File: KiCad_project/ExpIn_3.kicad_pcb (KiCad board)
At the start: 2 copper layers, 41 x 27 mm, 30 parts, among them J1 NMJ6HCD2, J2 Conn_01x08_MountingPin, J3 Conn_01x02_MountingPin, SW1 SW_Push, U1 74HC4066, U2 MCP6001-OT, U3 MCP4018T-103E/LT, U5 USBLC6-2SC6

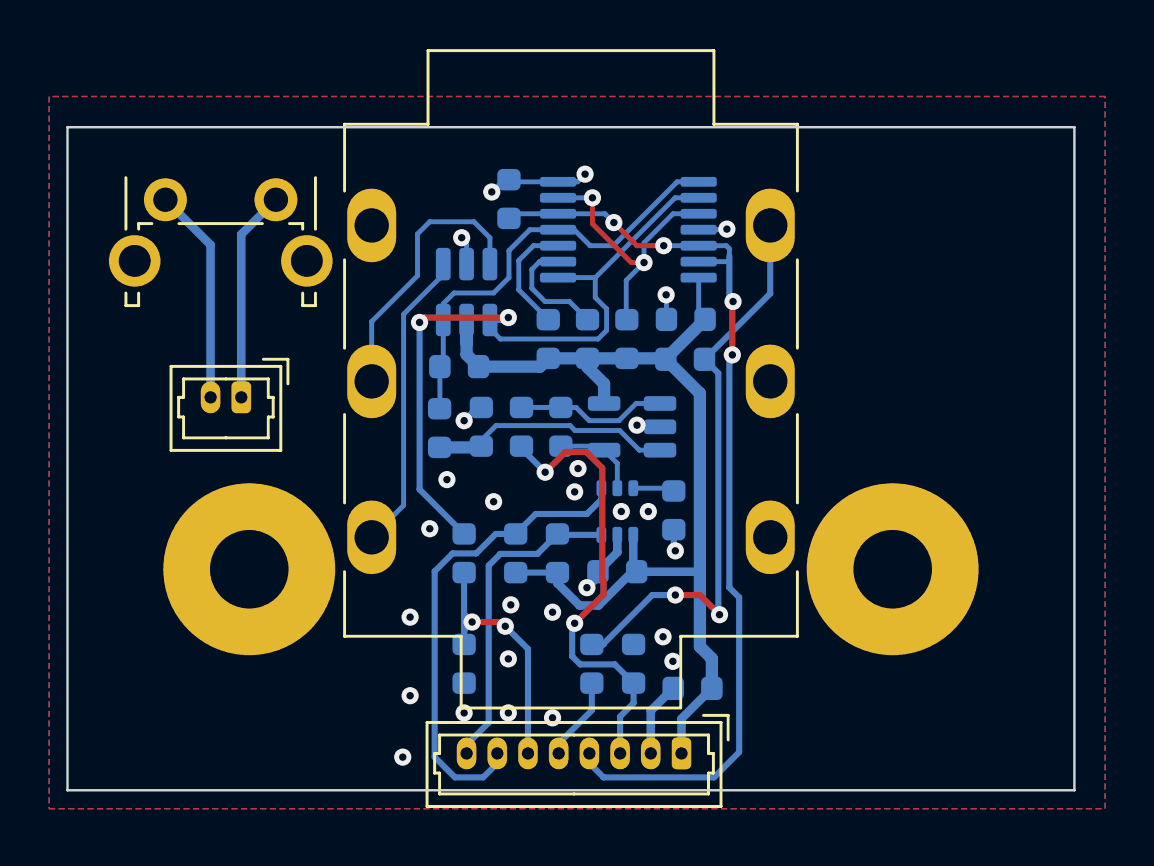
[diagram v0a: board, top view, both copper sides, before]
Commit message: SMT connectors, gain control
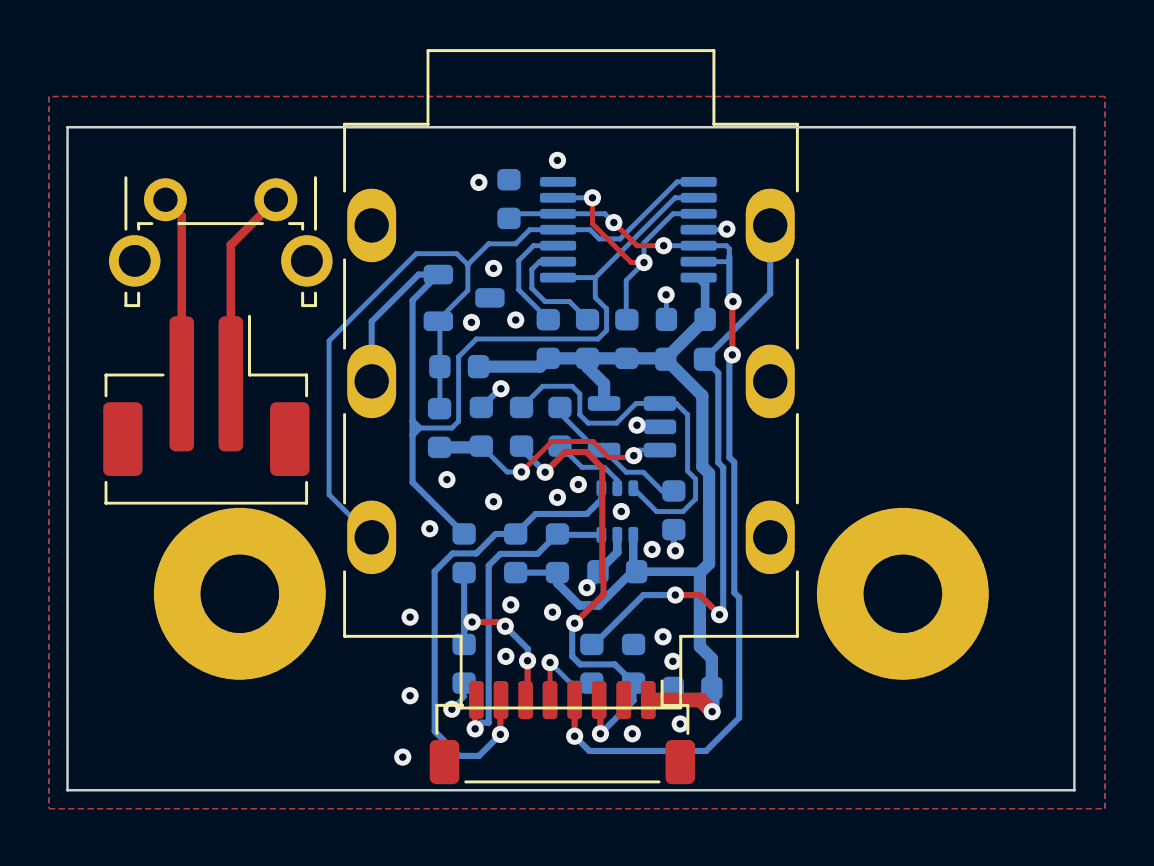
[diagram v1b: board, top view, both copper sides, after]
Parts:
- removed U5: USBLC6-2SC6, Package_TO_SOT_SMD:SOT-23-6
- added D1: PESD3V3L2BT, H_SOT:SOT-23, B.Cu at (89.9, 120.2)
- J2: footprint Connector_Molex:Molex_PicoBlade_53047-0810_1x08_P1.25mm_Vertical -> Connector_JST:JST_SH_BM08B-SRSS-TB_1x08-1MP_P1.00mm_Vertical
- J3: footprint Connector_Molex:Molex_PicoBlade_53047-0210_1x02_P1.25mm_Vertical -> Connector_JST:JST_PH_B2B-PH-SM4-TB_1x02-1MP_P2.00mm_Vertical
- R4: value 10k -> 1k
- moved J2 4.92 mm to (93.9, 137.9)
- moved J3 1.43 mm to (79.4, 124.2)
- moved H2 1.08 mm to (107.8, 132.2)
- moved H1 1.07 mm to (80.8, 132.2)
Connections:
- R1 pad 2: Net-(R1-Pad2) -> /T_IN
- R3 pad 1: Net-(R1-Pad2) -> /T_IN
- R4 pad 1: Net-(R4-Pad1) -> Net-(U2--)
- R4 pad 2: Net-(U2--) -> Net-(U3-W)
- R5 pad 1: Net-(U3-A) -> Net-(U2--)
- R6 pad 1: Net-(R4-Pad1) -> Net-(U3-A)
- R9 pad 2: Net-(R9-Pad2) -> /R_IN
- U1 pad 1: Net-(R9-Pad2) -> /R_IN
- U1 pad 4: Net-(R1-Pad2) -> /T_IN
- U1 pad 8: Net-(R1-Pad2) -> /T_IN
- U1 pad 9: Net-(R9-Pad2) -> /R_IN
- U2 pad 1: Net-(R4-Pad1) -> Net-(U3-A)
- U3 pad 5: Net-(U2--) -> Net-(U3-W)
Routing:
- net Net-(R9-Pad2): track 29.3 -> 0.00 mm, vias 2 -> 0
- net /R_IN: track 11.3 -> 39.9 mm
- net /T_IN: track 12.3 -> 33.7 mm
- net Net-(R1-Pad2): track 18.0 -> 0.00 mm
- net Net-(U3-A): track 1.70 -> 15.5 mm
- net GND: track 16.0 -> 9.08 mm, vias 27 -> 29
- net Net-(R4-Pad1): track 6.15 -> 0.00 mm
- net Net-(U3-W): track 0.00 -> 3.20 mm
- net Net-(U2--): track 3.60 -> 6.33 mm
- net Vcc: track 44.8 -> 42.6 mm, vias 0 -> 1
- net RSin: track 10.9 -> 8.76 mm, vias 2 -> 3
- net ADC: track 18.7 -> 19.6 mm, vias 2 -> 3
- net Net-(J3-Pin_2): track 8.81 -> 7.91 mm
- net /EXP_LP: track 9.90 -> 10.3 mm, vias 0 -> 2
- net TRctrl: track 39.1 -> 39.5 mm, vias 4 -> 5
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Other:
- board text added: "8pin connector + TRS jack: footprint courtyard violation, possible mechanical issues"

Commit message: board size update, dec. caps 1u, bom
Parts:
- C1: value 10u -> 1u
- C4, C5: value 100n -> 1u
- moved J2 0.97 mm to (93.9, 138.9)
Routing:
- net Sense: track 3.57 -> 4.55 mm
- net RSin: track 8.76 -> 9.73 mm
- net ADC: track 19.6 -> 20.3 mm
- net SCL: track 13.4 -> 14.0 mm
- net GND: vias 29 -> 31
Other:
- board size 41 x 27 mm -> 41 x 28.1 mm
- board text removed: "8pin connector + TRS jack: footprint courtyard violation, possible mechanical issues"
